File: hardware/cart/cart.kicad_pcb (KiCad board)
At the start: 2 copper layers, 40.1 x 34.8 mm, 8 parts, among them J1 Front Edge, J2 Back Edge, U1 Pro Micro

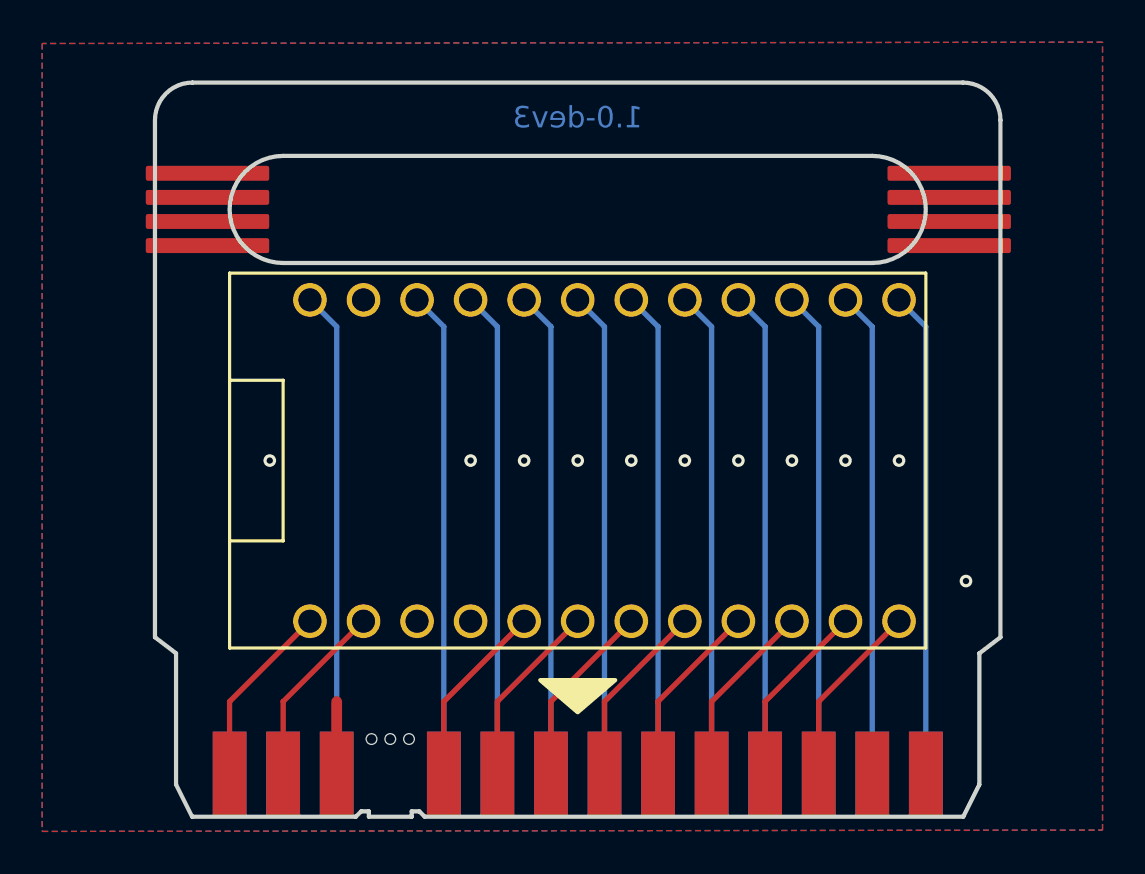
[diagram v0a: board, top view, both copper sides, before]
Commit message: Rename to dotMG
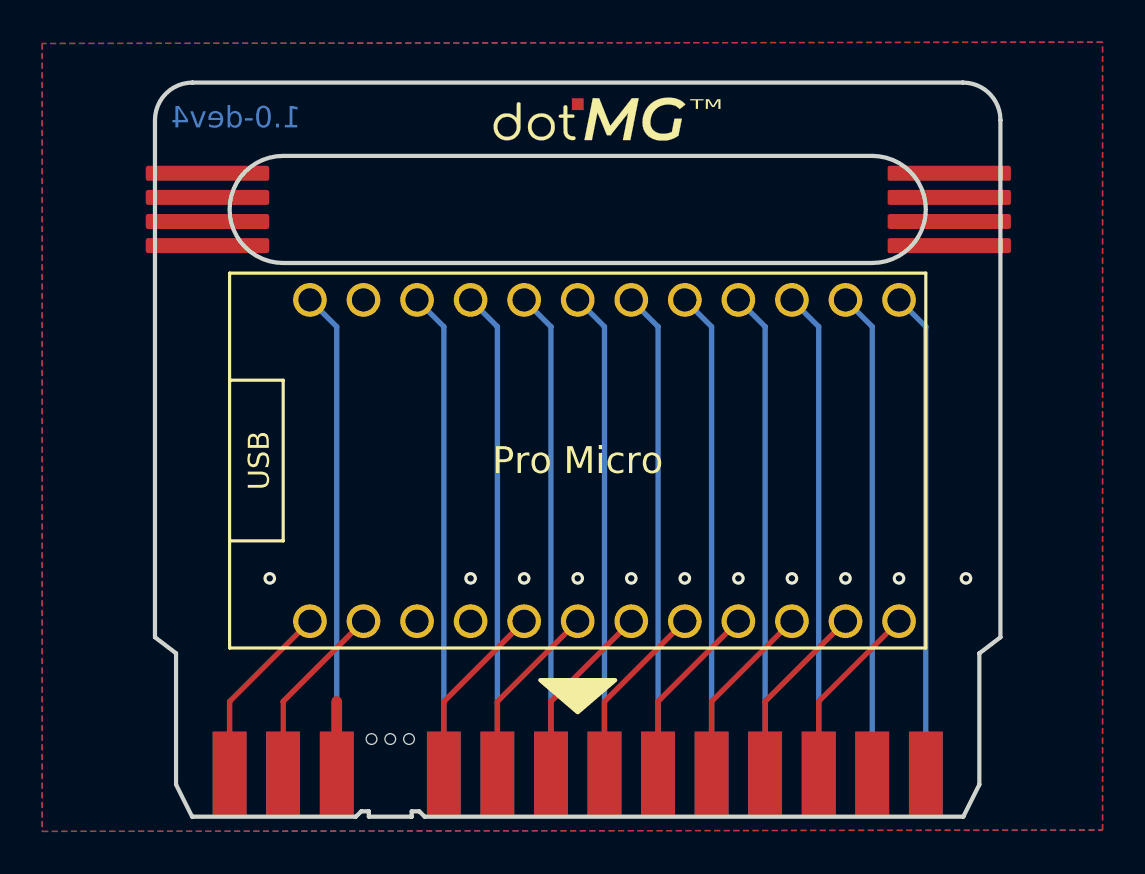
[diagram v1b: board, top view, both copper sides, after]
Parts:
- added G***: LOGO, cart:LOGO, F.Cu at (139.7, 94.9)
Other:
- board text added: "1.0-dev4"
- board text added: "USB"
- board text added: "dotMG (Pro Micro) Cart"
- board text added: "github.com/menehune23/arduboy-dotmg"
- board text removed: "1.0-dev3"
- board text removed: "Arduboy CE Cart"
- board text removed: "Designed by John, Nathan, and Andrew Meyer"
- board text removed: "github.com/menehune23/arduboy-ce"
